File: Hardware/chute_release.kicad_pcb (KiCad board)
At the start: 4 copper layers, 19.3 x 28.2 mm, 51 parts, among them J2 Conn_01x03, J3 Conn_01x02_Pin, J4 USB4105-GF-A, Q1 DMG3415UFY4Q-7, SW1 SH-7050TB, SW2 SW_Push, SW3 SW_Push, U1 AP7361C-33E, U2 W25Q128JVS, U3 RP2040, U4 DPS310XTSA1, U5 MCP73831-2-OT, Y1 ABM8-272-T3

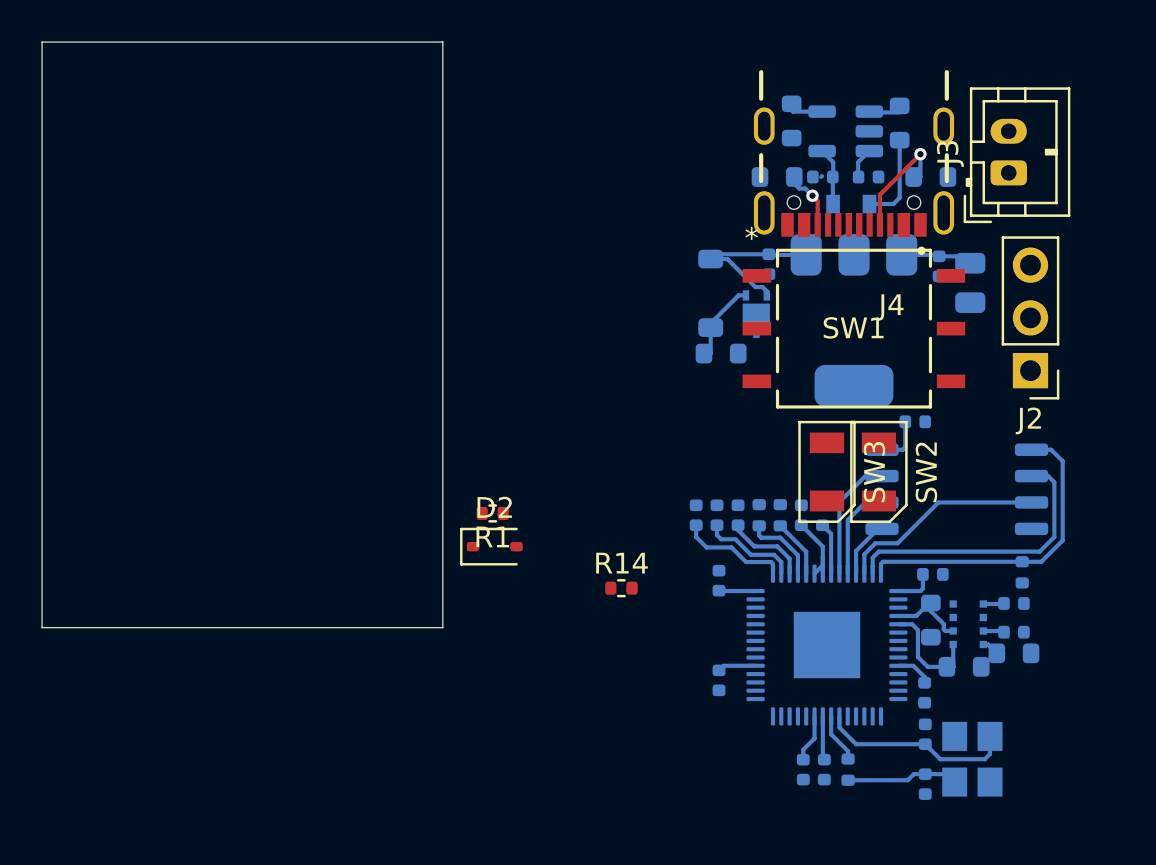
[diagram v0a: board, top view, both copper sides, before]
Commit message: Pretty much finished pcb routing
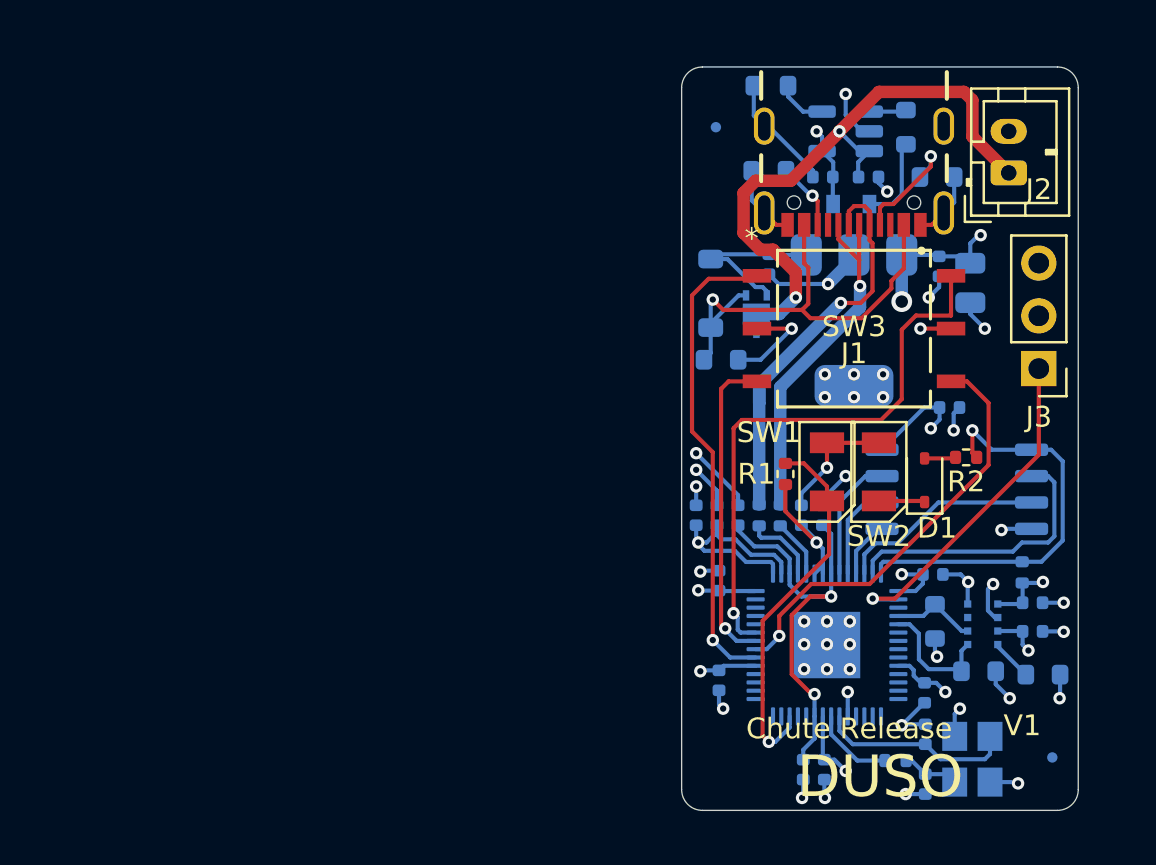
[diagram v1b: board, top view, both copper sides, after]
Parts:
- added REF**: Fiducial_0.5mm_Mask1.5mm, Fiducial:Fiducial_0.5mm_Mask1.5mm, B.Cu at (118.2, 83.7)
- added REF**: Fiducial_0.5mm_Mask1.5mm, Fiducial:Fiducial_0.5mm_Mask1.5mm, B.Cu at (134.3, 114.0)
- moved R2 23.0 mm to (130.2, 99.6)
- moved D1 20.9 mm to (128.2, 100.7), turned to 90 degrees
- moved R1 9.63 mm to (121.5, 100.4), turned to 90 degrees
- moved R10 2.33 mm to (126.8, 114.2), turned to 0 degrees
- moved R4 1.97 mm to (120.8, 81.7), turned to 180 degrees
- moved C8 1.79 mm to (129.4, 97.2)
- moved R7 1.73 mm to (133.9, 110.1)
- moved C12 0.90 mm to (133.4, 108.0)
- moved C7 0.90 mm to (133.4, 106.6)
- moved R8 0.73 mm to (130.8, 109.9)
- moved U5 0.70 mm to (131.0, 107.6)
- moved R3 0.50 mm to (120.7, 85.8)
- moved J3 0.41 mm to (133.7, 95.3)
- moved R6 0.36 mm to (127.3, 83.7)
- moved R11 0.30 mm to (118.4, 94.9)
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- renumbered C17 to C1, C16 to C10, C15 to C11, C19 to C12, C12 to C13, C7 to C14, C5 to C15, C1 to C16, C10 to C17, C9 to C18, C14 to C19, C13 to C2, C2 to C20, C8 to C21, C11 to C5, C21 to C6, C18 to C7, C6 to C8, C20 to C9, D2 to D1, D1 to D2, J4 to J1, J3 to J2, J2 to J3, R14 to R1, R3 to R10, R10 to R11, R4 to R12, R5 to R13, R2 to R14, R1 to R2, R11 to R3, R12 to R4, R9 to R5, R13 to R6, R8 to R7, R7 to R8, R6 to R9, SW3 to SW1, SW1 to SW3, U5 to U1, U1 to U2, U2 to U3, U3 to U4, U4 to U5
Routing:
- net GND: track 0.00 -> 66.0 mm, vias 0 -> 43
- net +BATT: track 1.48 -> 29.4 mm, vias 0 -> 2
- net HEX_SW_8: track 0.00 -> 27.3 mm, vias 0 -> 1
- net +3V3: track 33.8 -> 57.0 mm, vias 0 -> 15
- net HEX_SW_1: track 0.00 -> 22.9 mm, vias 0 -> 1
- net HEX_SW_2: track 0.00 -> 20.7 mm, vias 0 -> 1
- net USB_D-: track 0.00 -> 19.8 mm, vias 0 -> 1
- net VBUS: track 3.72 -> 22.7 mm, vias 0 -> 1
- net /MCU/RUN: track 0.00 -> 18.1 mm, vias 0 -> 1
- net USB_D+: track 0.00 -> 17.2 mm, vias 0 -> 1
- net /MCU/GPIO0: track 0.00 -> 16.3 mm, vias 0 -> 1
- net HEX_SW_4: track 0.00 -> 15.2 mm, vias 0 -> 1
- net +1V1: track 8.82 -> 20.4 mm, vias 0 -> 2
- net /MCU/QSPI_SS: track 15.2 -> 19.9 mm, vias 0 -> 1
- net Net-(C2-Pad1): track 5.41 -> 2.77 mm
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- removed copper zone on In2.Cu, net GND
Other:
- board size 19.3 x 28.2 mm -> 19.1 x 35.8 mm
- board text added: "Chute Release"
- board text added: "DUSO"
- board text added: "V1"

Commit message: updated routing
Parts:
- removed REF** (x2): Fiducial_0.5mm_Mask1.5mm, Fiducial:Fiducial_0.5mm_Mask1.5mm
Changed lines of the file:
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@@
 		(tags "resistor")
 		(property "Reference" "R4"
-			(at 2.4 -0.1 360)
+			(at 2.4 -0.1 0)
 			(layer "B.SilkS")
 			(effects
@@
 		)
 		(property "Value" "10k"
-			(at 0 -1.43 360)
+			(at 0 -1.43 0)
 			(layer "B.Fab")
 			(effects
@@
 		)
 		(fp_text user "${REFERENCE}"
-			(at 0 0 360)
+			(at 0 0 0)
 			(layer "B.Fab")
 			(effects
@@
 		)
 	)
-	(footprint "Fiducial:Fiducial_0.5mm_Mask1.5mm"
-		(layer "B.Cu")
-		(at 118.15 83.7 180)
-		(descr "Circular Fiducial, 0.5mm bare copper, 1.5mm soldermask opening")
-		(tags "fiducial")
-		(property "Reference" "REF**"
-			(at 0 1.7145 0)
-			(layer "B.SilkS")
-			(hide yes)
-			(effects
-				(font
-					(size 1 1)
-					(thickness 0.15)
-				)
-				(justify mirror)
-			)
-		)
-		(property "Value" "Fiducial_0.5mm_Mask1.5mm"
-			(at 0 -1.7145 0)
-			(layer "B.Fab")
-			(effects
-				(font
-					(size 1 1)
-					(thickness 0.15)
-				)
-				(justify mirror)
-			)
-		)
-		(property "Footprint" "Fiducial:Fiducial_0.5mm_Mask1.5mm"
-			(at 0 0 0)
-			(unlocked yes)
-			(layer "B.Fab")
-			(hide yes)
-			(effects
-				(font
-					(size 1.27 1.27)
-					(thickness 0.15)
-				)
-				(justify mirror)
-			)
-		)
-		(property "Datasheet" ""
-			(at 0 0 0)
-			(unlocked yes)
-			(layer "B.Fab")
-			(hide yes)
-			(effects
-				(font
-					(size 1.27 1.27)
-					(thickness 0.15)
-				)
-				(justify mirror)
-			)
-		)
-		(property "Description" ""
-			(at 0 0 0)
-			(unlocked yes)
-			(layer "B.Fab")
-			(hide yes)
-			(effects
-				(font
-					(size 1.27 1.27)
-					(thickness 0.15)
-				)
-				(justify mirror)
-			)
-		)
-		(attr smd)
-		(fp_circle
-			(center 0 0)
-			(end 1 0)
-			(stroke
-				(width 0.05)
-				(type solid)
-			)
-			(fill none)
-			(layer "B.CrtYd")
-		)
-		(fp_circle
-			(center 0 0)
-			(end 0.75 0)
-			(stroke
-				(width 0.1)
-				(type solid)
-			)
-			(fill none)
-			(layer "B.Fab")
-		)
-		(fp_text user "${REFERENCE}"
-			(at 0 0 0)
-			(layer "B.Fab")
-			(effects
-				(font
-					(size 0.2 0.2)
-					(thickness 0.04)
-				)
-				(justify mirror)
-			)
-		)
-		(pad "" smd circle
-			(at 0 0 180)
-			(size 0.5 0.5)
-			(layers "B.Cu" "B.Mask")
-			(solder_mask_margin 0.5)
-			(clearance 0.5)
-		)
-	)
 	(footprint "Package_DFN_QFN:QFN-56-1EP_7x7mm_P0.4mm_EP3.2x3.2mm"
 		(layer "B.Cu")
@@
 		(tags "resistor")
 		(property "Reference" "R10"
-			(at -0.4 1.1 360)
+			(at -0.4 1.1 0)
 			(layer "B.SilkS")
 			(effects
@@
 		)
 		(property "Value" "1k"
-			(at 0 -1.17 360)
+			(at 0 -1.17 0)
 			(layer "B.Fab")
 			(effects
@@
 		)
 		(fp_text user "${REFERENCE}"
-			(at 0 0 360)
+			(at 0 0 0)
 			(layer "B.Fab")
 			(effects
@@
 		)
 	)
-	(footprint "Fiducial:Fiducial_0.5mm_Mask1.5mm"
-		(layer "B.Cu")
-		(at 134.35 114.05 180)
-		(descr "Circular Fiducial, 0.5mm bare copper, 1.5mm soldermask opening")
-		(tags "fiducial")
-		(property "Reference" "REF**"
-			(at 3.5 -0.2 0)
-			(layer "B.SilkS")
-			(hide yes)
-			(effects
-				(font
-					(size 1 1)
-					(thickness 0.15)
-				)
-				(justify mirror)
-			)
-		)
-		(property "Value" "Fiducial_0.5mm_Mask1.5mm"
-			(at 0 -1.7145 0)
-			(layer "B.Fab")
-			(effects
-				(font
-					(size 1 1)
-					(thickness 0.15)
-				)
-				(justify mirror)
-			)
-		)
-		(property "Footprint" "Fiducial:Fiducial_0.5mm_Mask1.5mm"
-			(at 0 0 0)
-			(unlocked yes)
-			(layer "B.Fab")
-			(hide yes)
-			(effects
-				(font
-					(size 1.27 1.27)
-					(thickness 0.15)
-				)
-				(justify mirror)
-			)
-		)
-		(property "Datasheet" ""
-			(at 0 0 0)
-			(unlocked yes)
-			(layer "B.Fab")
-			(hide yes)
-			(effects
-				(font
-					(size 1.27 1.27)
-					(thickness 0.15)
-				)
-				(justify mirror)
-			)
-		)
-		(property "Description" ""
-			(at 0 0 0)
-			(unlocked yes)
-			(layer "B.Fab")
-			(hide yes)
-			(effects
-				(font
-					(size 1.27 1.27)
-					(thickness 0.15)
-				)
-				(justify mirror)
-			)
-		)
-		(attr smd)
-		(fp_circle
-			(center 0 0)
-			(end 1 0)
-			(stroke
-				(width 0.05)
-				(type solid)
-			)
-			(fill none)
-			(layer "B.CrtYd")
-		)
-		(fp_circle
-			(center 0 0)
-			(end 0.75 0)
-			(stroke
-				(width 0.1)
-				(type solid)
-			)
-			(fill none)
-			(layer "B.Fab")
-		)
-		(fp_text user "${REFERENCE}"
-			(at 0 0 0)
-			(layer "B.Fab")
-			(effects
-				(font
-					(size 0.2 0.2)
-					(thickness 0.04)
-				)
-				(justify mirror)
-			)
-		)
-		(pad "" smd circle
-			(at 0 0 180)
-			(size 0.5 0.5)
-			(layers "B.Cu" "B.Mask")
-			(solder_mask_margin 0.5)
-			(clearance 0.5)
-		)
-	)

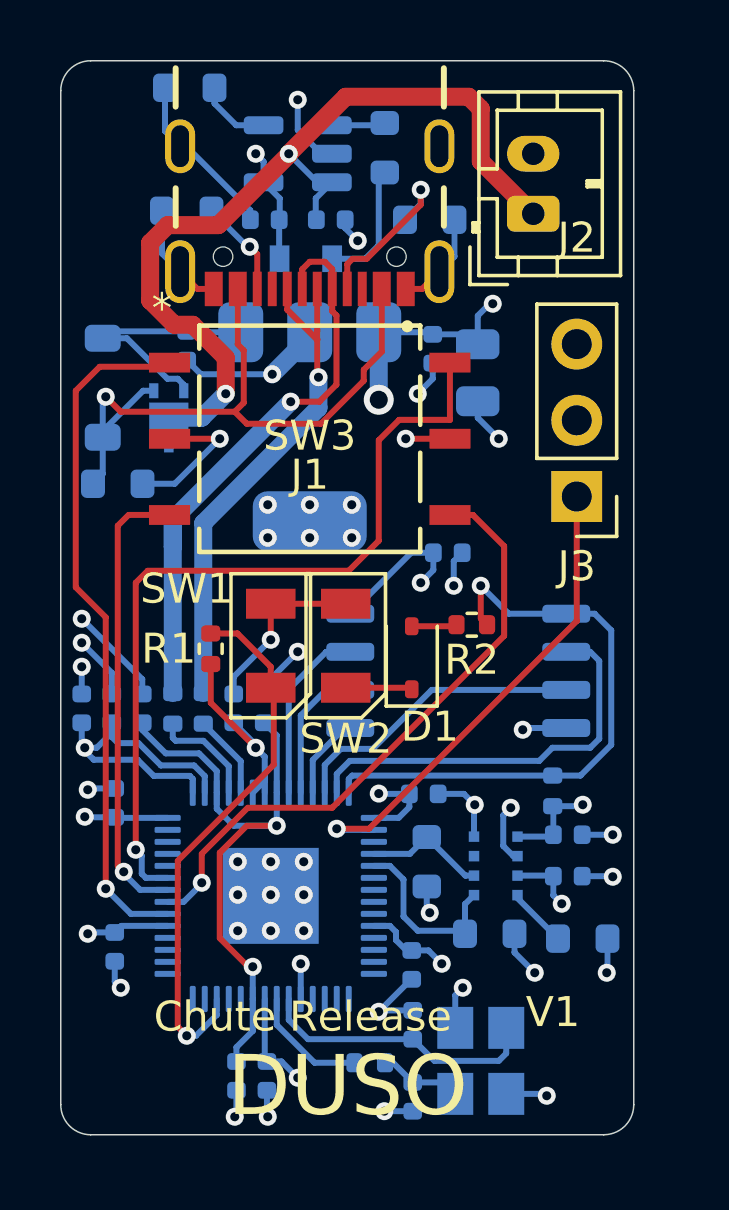
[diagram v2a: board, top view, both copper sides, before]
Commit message: Added new components to sch and pcb and redid the routing and layout of pcb
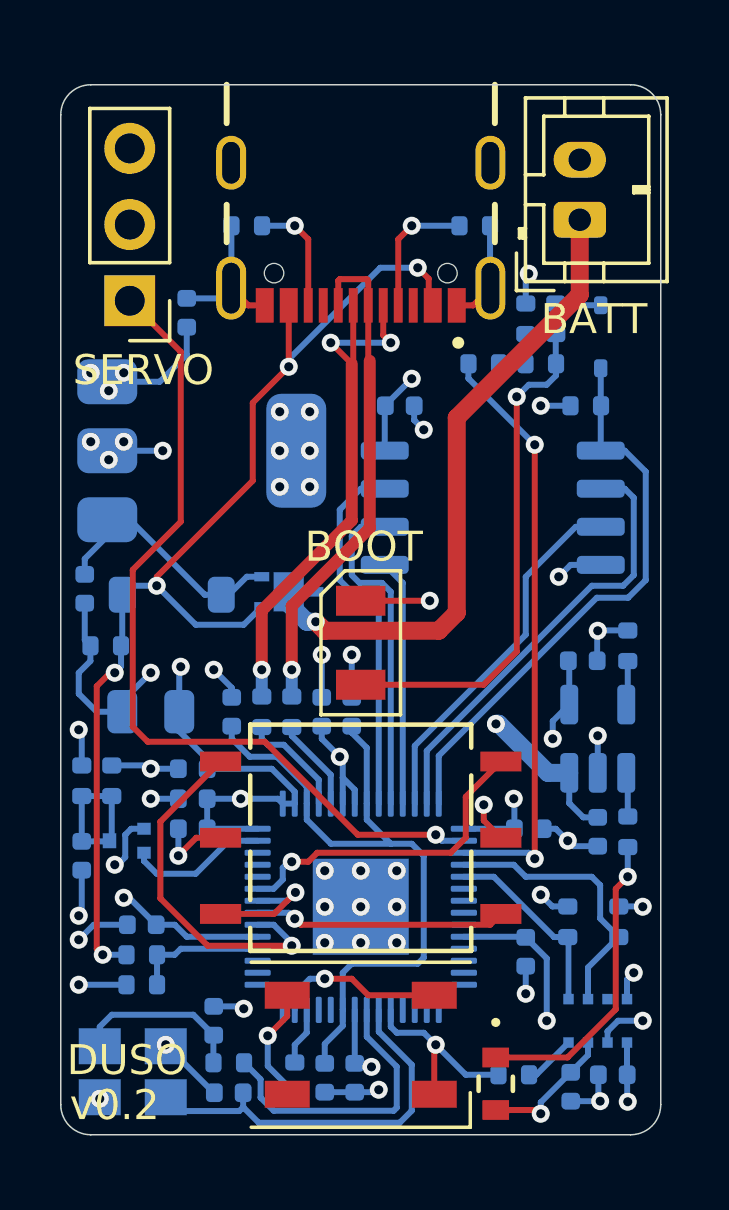
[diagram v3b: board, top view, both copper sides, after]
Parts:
- removed CR1: TLMS1100-GS08, duso:LED_VISHAY_TLMX1100_VIS
- removed SW2: SW_Push, duso:NanoT-AS
- removed SW3: SH-7050TB, duso:SH-7050B_NDC
- added BOOT: SW_Push, duso:NanoT-AS, F.Cu at (126.5, 100.2)
- added C22: 100n, Capacitor_SMD:C_0402_1005Metric, B.Cu at (134.9, 114.6)
- added CHR1: TLMS1100-GS08, duso:LED_VISHAY_TLMX1100_VIS, F.Cu at (131.0, 114.9)
- added D3: WS2812B, LED_SMD:LED_WS2812B_PLCC4_5.0x5.0mm_P3.2mm, F.Cu at (126.5, 113.6)
- added Q2: SSM3K35AMFV_L3F, duso:VESM_SOT-723_, B.Cu at (118.7, 106.8)
- added R15: 1M5, Resistor_SMD:R_0402_1005Metric, B.Cu at (117.2, 104.8)
- added R16: 750k, Resistor_SMD:R_0402_1005Metric, B.Cu at (118.2, 104.8)
- added R17: 5k, Resistor_SMD:R_0402_1005Metric, B.Cu at (135.4, 100.3)
- added R18: 10k, Resistor_SMD:R_0402_1005Metric, B.Cu at (135.4, 106.5)
- added R19: 10k, Resistor_SMD:R_0402_1005Metric, B.Cu at (135.1, 109.5)
- added R20: 10k, Resistor_SMD:R_0402_1005Metric, B.Cu at (133.4, 109.5)
- added R21: 100k, Resistor_SMD:R_0402_1005Metric, B.Cu at (131.6, 114.6)
- C1: value 10u -> 15p
- C11: value 100n -> 10u; footprint Capacitor_SMD:C_0402_1005Metric -> Capacitor_SMD:C_0805_2012Metric
- C14, C8, C9: value 100n -> 4.7u
- C15: value 10u -> 100n; footprint Capacitor_SMD:C_0805_2012Metric -> Capacitor_SMD:C_0402_1005Metric
- C16, C20: value 15p -> 100n
- C18: value 1u -> 10u
- C2: value 4.7u -> 15p
- C3, C4: value 4.7u -> 100n
- C5: value 1u -> 100n
- C6, C7: value 100n -> 1u
- D1, R1, R2: moved to B.Cu
- J1: value USB4105-GF-A -> Conn_01x03; footprint duso:GCT_USB4105-GF-A -> Connector_PinHeader_2.54mm:PinHeader_1x03_P2.54mm_Vertical
- J3: value Conn_01x03 -> USB4105-GF-A; footprint Connector_PinHeader_2.54mm:PinHeader_1x03_P2.54mm_Vertical -> duso:GCT_USB4105-GF-A
- R10: value 1k -> 5k
- R11, R4: footprint Resistor_SMD:R_0603_1608Metric -> Resistor_SMD:R_0402_1005Metric
- R12: value 27 -> 5k
- R13: value 27 -> 5k6
- R3, R5: value 5k -> 10k; footprint Resistor_SMD:R_0603_1608Metric -> Resistor_SMD:R_0402_1005Metric
- R6: value 10k -> 1k; footprint Resistor_SMD:R_0603_1608Metric -> Resistor_SMD:R_0402_1005Metric
- R7: value 100k -> 10k; footprint Resistor_SMD:R_0603_1608Metric -> Resistor_SMD:R_0402_1005Metric
- R8, R9: value 10k -> 27; footprint Resistor_SMD:R_0603_1608Metric -> Resistor_SMD:R_0402_1005Metric
- SW1: value SW_Push -> SH-7050TB; footprint duso:NanoT-AS -> duso:SH-7050B_NDC
- U1: value MCP73831-2-OT -> W25Q128JVS; footprint Package_TO_SOT_SMD:SOT-23-5 -> Package_SO:SOIC-8_5.23x5.23mm_P1.27mm
- U2: value AP7361C-33E -> RP2040; footprint Package_TO_SOT_SMD:SOT-223-3_TabPin2 -> Package_DFN_QFN:QFN-56-1EP_7x7mm_P0.4mm_EP3.2x3.2mm
- U3: value W25Q128JVS -> AP7361C-33E; footprint Package_SO:SOIC-8_5.23x5.23mm_P1.27mm -> Package_TO_SOT_SMD:SOT-223-3_TabPin2
- U4: value RP2040 -> MCP73831-2-OT; footprint Package_DFN_QFN:QFN-56-1EP_7x7mm_P0.4mm_EP3.2x3.2mm -> Package_TO_SOT_SMD:SOT-23-5
- moved C1 29.3 mm to (122.1, 115.2), turned to 180 degrees
- moved R10 28.1 mm to (130.3, 86.3)
- moved C2 26.8 mm to (121.6, 112.8), turned to 90 degrees
- moved C15 23.9 mm to (126.3, 114.7)
- moved R2 16.7 mm to (122.1, 114.2)
- moved R12 16.2 mm to (122.7, 86.3), turned to 180 degrees
- moved U2 16.1 mm to (126.5, 109.0), turned to 180 degrees
- moved C18 15.7 mm to (134.4, 106.5), turned to -90 degrees
- moved R14 15.1 mm to (119.2, 111.6), turned to 180 degrees
- moved R1 14.9 mm to (134.0, 92.3), turned to 0 degrees
- moved C13 14.6 mm to (132.0, 110.5), turned to -90 degrees
- moved C5 14.2 mm to (125.3, 114.7), turned to -90 degrees
- moved C9 13.6 mm to (120.7, 89.2)
- moved U1 13.5 mm to (130.9, 95.7)
- moved R4 13.4 mm to (130.6, 90.9)
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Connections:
- C1 pad 1: +BATT -> /MCU/XIN
- C10 pad 1: +3V3 -> Net-(C10-Pad1)
- C14 pad 1: +1V1 -> +3V3
- C16 pad 1: /MCU/XIN -> +3V3
- C18 pad 1: +1V1 -> +BATT
- C2 pad 1: +3V3 -> Net-(C2-Pad1)
- C20 pad 1: Net-(C2-Pad1) -> +3V3
- C21 pad 1: +1V1 -> +3V3
- C3 pad 1: Net-(D1-K) -> +3V3
- C4 pad 1: +3V3 -> +1V1
- C5 pad 1: +3V3 -> +1V1
- C6 pad 1: +3V3 -> +1V1
- C8 pad 1: +3V3 -> Net-(D2-K)
- D1 pad 1: Net-(D2-K) -> Net-(D1-K)
- D1 pad 2: Net-(D2-A) -> /MCU/QSPI_SS
- D2 pad 1: Net-(D1-K) -> Net-(D2-K)
- Q1 pad 2: Net-(D1-K) -> Net-(D2-K)
- R1 pad 2: /MCU/RUN -> /MCU/QSPI_SS
- R10 pad 1: /MCU/XOUT -> Net-(J3-CC1)
- R10 pad 2: Net-(C2-Pad1) -> GND
- R12 pad 1: USB_D+ -> Net-(J3-CC2)
- R12 pad 2: Net-(U3-USB_DP) -> GND
- R13 pad 1: USB_D- -> VBUS
- R13 pad 2: Net-(U3-USB_DM) -> VBUS_DETECT
- R14 pad 1: +3V3 -> VBUS_DETECT
- R14 pad 2: /MCU/QSPI_SS -> GND
- R2 pad 1: /MCU/QSPI_SS -> /MCU/XOUT
- R2 pad 2: Net-(D2-A) -> Net-(C2-Pad1)
- R3 pad 1: Net-(J4-CC2) -> Net-(BOOT1-Pad2)
- R3 pad 2: GND -> Net-(R3-Pad2)
- R4 pad 1: Net-(U5-PROG) -> Net-(R3-Pad2)
- R4 pad 2: GND -> /MCU/USER_SW
- R5 pad 1: Net-(J4-CC1) -> +3V3
- R5 pad 2: GND -> Net-(BOOT1-Pad2)
- R6 pad 1: Net-(CR1-Pad1) -> Net-(BOOT1-Pad2)
- R6 pad 2: Net-(U5-STAT) -> Net-(D1-K)
- R7 pad 1: SDO -> +3V3
- R7 pad 2: GND -> /MCU/RUN
- R8 pad 1: +3V3 -> USB_D+
- R8 pad 2: SDK -> Net-(U2-USB_DP)
- R9 pad 1: +3V3 -> USB_D-
- R9 pad 2: SDI -> Net-(U2-USB_DM)
- SW1 pad 1: /MCU/RUN -> HEX_SW_1
- U1 pad 1: Net-(U5-STAT) -> /MCU/QSPI_SS
- U1 pad 2: GND -> /MCU/QSPI_SD1
- U1 pad 3: +BATT -> /MCU/QSPI_SD2
- U1 pad 4: +3V3 -> GND
- U1 pad 5: Net-(U5-PROG) -> /MCU/QSPI_SD0
- U2 pad 1: Net-(D1-K) -> +3V3
- U2 pad 2: GND -> /MCU/GPIO0
- U2 pad 3: +3V3 -> /MCU/USER_SW
- U3 pad 1: /MCU/QSPI_SS -> Net-(D2-K)
- U3 pad 2: /MCU/QSPI_SD1 -> GND
- U3 pad 3: /MCU/QSPI_SD2 -> +3V3
- U4 pad 1: +3V3 -> Net-(U4-STAT)
- U4 pad 2: /MCU/GPIO0 -> GND
- U4 pad 3: /MCU/GPIO1 -> +BATT
- U4 pad 4: SDI -> +3V3
- U4 pad 5: SDK -> Net-(U4-PROG)
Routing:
- net /MCU/USER_SW: track 0.00 -> 19.9 mm, vias 0 -> 2
- net Net-(BOOT1-Pad2): track 0.00 -> 18.1 mm, vias 0 -> 1
- net HEX_SW_8: track 27.3 -> 10.9 mm
- net /MCU/RUN: track 18.1 -> 1.92 mm, vias 1 -> 0
- net VBUS: track 22.7 -> 37.3 mm, vias 1 -> 5
- net HEX_SW_2: track 20.7 -> 8.43 mm
- net /MCU/GPIO0: track 16.3 -> 28.2 mm
- net HEX_SW_4: track 15.2 -> 4.17 mm
- net HEX_SW_1: track 22.9 -> 11.9 mm
- net Net-(CHR1-Pad1): track 0.00 -> 10.2 mm, vias 0 -> 1
- net Net-(D1-K): track 8.25 -> 1.52 mm
- net /MCU/QSPI_SCLK: track 4.58 -> 11.1 mm
- net /MCU/QSPI_SD3: track 6.02 -> 12.4 mm
- net Net-(D2-K): track 2.22 -> 8.56 mm
- net /MCU/XOUT: track 3.98 -> 9.83 mm
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- added copper zone on In2.Cu, net +BATT
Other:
- board size 19.1 x 35.8 mm -> 20 x 35 mm
- board text added: "BATT"
- board text added: "SERVO"
- board text added: "v0.2"
- board text removed: "Chute Release"
- board text removed: "V1"
